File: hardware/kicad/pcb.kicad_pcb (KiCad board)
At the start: 2 copper layers, 133 x 73.5 mm, 14 parts, among them J1 ENCODER, J2 MOTOR, J3 12V MOTOR, U1 Dual_L298N_H_Bridge, U2 Level_Shifter

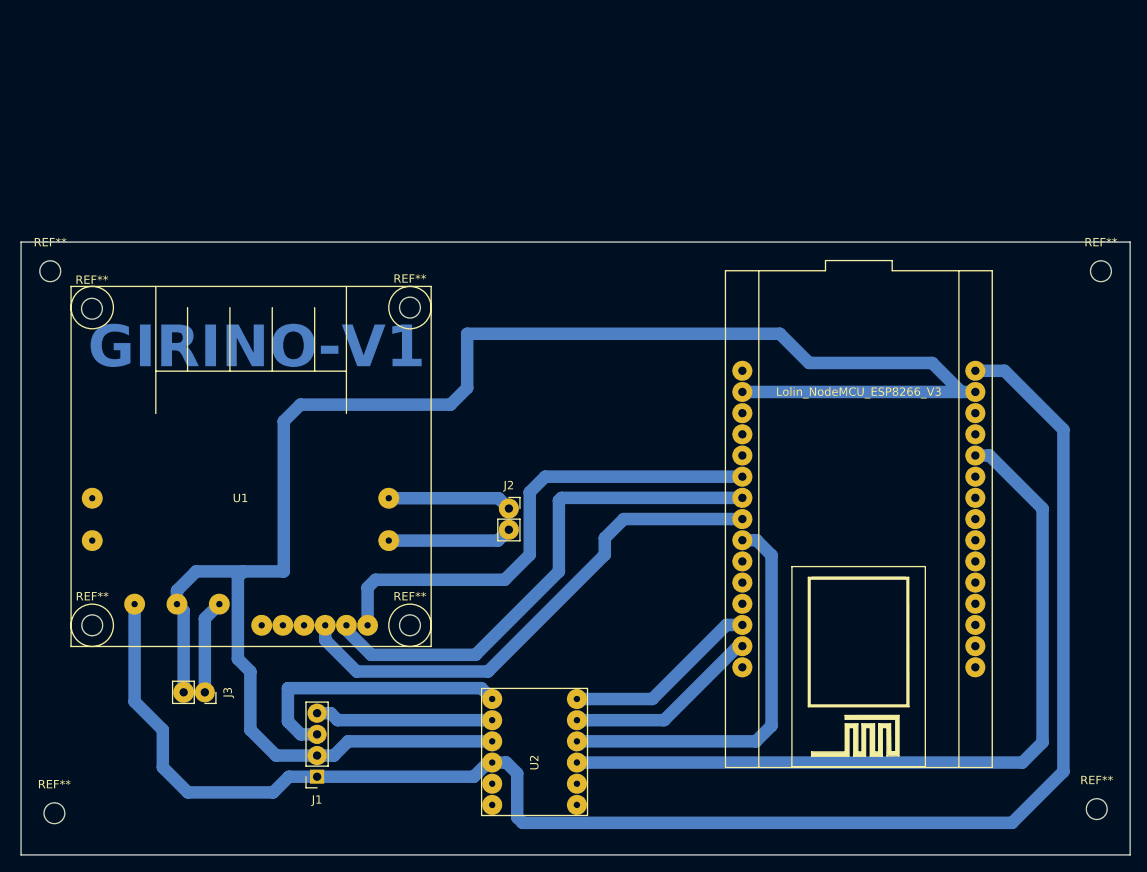
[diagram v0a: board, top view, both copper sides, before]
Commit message: fix : corrige erro de orientação nos arquivos gerber
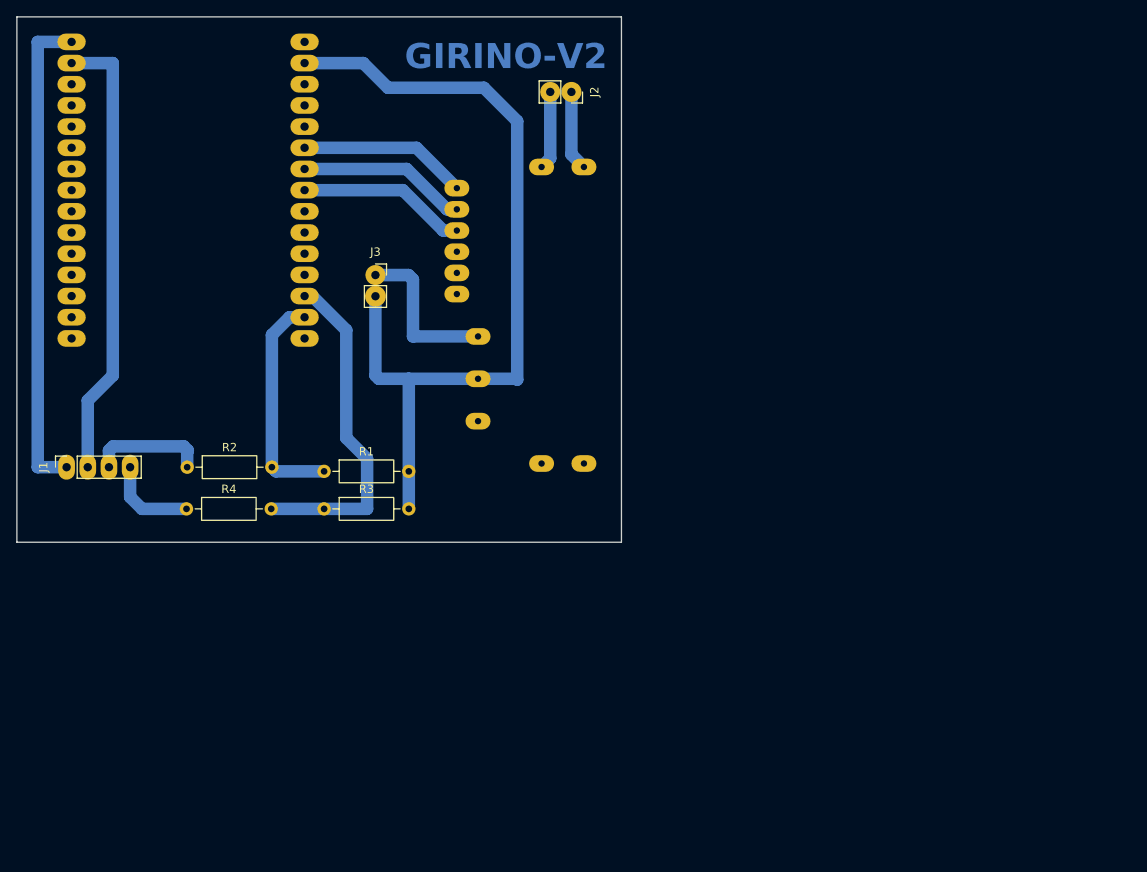
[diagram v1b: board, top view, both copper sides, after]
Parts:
- removed REF** (x8): MountingHole_2.5mm, MountingHole:MountingHole_2.5mm
- removed U2: Level_Shifter, megasaturnv_custom_components:Level_Shifter
- added R1: 3,3k, Resistor_THT:R_Axial_DIN0207_L6.3mm_D2.5mm_P10.16mm_Horizontal, F.Cu at (96.8, 95.5)
- added R2: 2,2k, Resistor_THT:R_Axial_DIN0207_L6.3mm_D2.5mm_P10.16mm_Horizontal, F.Cu at (80.4, 95.0)
- added R3: 3,3k, Resistor_THT:R_Axial_DIN0207_L6.3mm_D2.5mm_P10.16mm_Horizontal, F.Cu at (96.8, 100.0)
- added R4: 2,2k, Resistor_THT:R_Axial_DIN0207_L6.3mm_D2.5mm_P10.16mm_Horizontal, F.Cu at (80.3, 100.0)
- A1, U1: moved to B.Cu
- moved A1 89.6 mm to (80.5, 61.8), turned to 180 degrees
- moved J3 54.1 mm to (103.0, 72.0), turned to 0 degrees
- moved J2 50.5 mm to (126.5, 50.0), turned to -90 degrees
- moved U1 47.8 mm to (110.2, 97.1), turned to 90 degrees
- moved J1 47.8 mm to (66.0, 95.0), turned to 90 degrees
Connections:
- A1 pad 17: Net-(U1-GND) -> unconnected-(A1-GND-Pad17)
- A1 pad 2: Net-(U1-GND) -> GND
- A1 pad 29: Net-(U1-GND) -> Net-(A1-GND-Pad29)
- A1 pad 9: Net-(A1-GND-Pad9) -> unconnected-(A1-GND-Pad9)
- J1 pad 2: Net-(U1-GND) -> Net-(A1-GND-Pad29)
- J3 pad 2: Net-(U1-GND) -> GND
- U1 pad 1: VIN -> unconnected-(U1-5v-Pad1)
- U1 pad 2: Net-(U1-GND) -> GND
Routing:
- net Net-(U1-GND): track 215.4 -> 0.00 mm
- net VIN: track 194.8 -> 58.5 mm
- net GND: track 0.00 -> 101.7 mm
- net +3.3V: track 95.6 -> 0.00 mm
- net Net-(A1-GND-Pad29): track 0.00 -> 54.6 mm
- net Net-(A1-GND-Pad9): track 48.8 -> 0.00 mm
- net Net-(A1-D5/GPIO14/SCLK): track 62.1 -> 20.3 mm
- net Net-(A1-D6/GPIO12/MISO): track 62.1 -> 20.3 mm
- net Net-(A1-D7/GPIO13/MOSI/RX2): track 59.4 -> 20.3 mm
- net Net-(J1-Pad3): track 33.2 -> 13.9 mm
- net Net-(A1-D2/GPIO4/SDA): track 23.5 -> 40.7 mm
- net Net-(J1-Pad4): track 21.3 -> 10.9 mm
- net Net-(U1-12v): track 11.3 -> 19.3 mm
- net Net-(U1-OUTB1): track 14.9 -> 9.43 mm
- net Net-(U1-OUTB2): track 14.9 -> 9.62 mm
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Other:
- board size 133 x 73.5 mm -> 72.5 x 63 mm
- board text added: "GIRINO-V2"
- board text removed: "GIRINO-V1"
